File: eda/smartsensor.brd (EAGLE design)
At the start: 33 x 27.9 mm, 46 parts, among them U1 ISL83491SOIC, U2 ATTINY1634, U3 3.3V

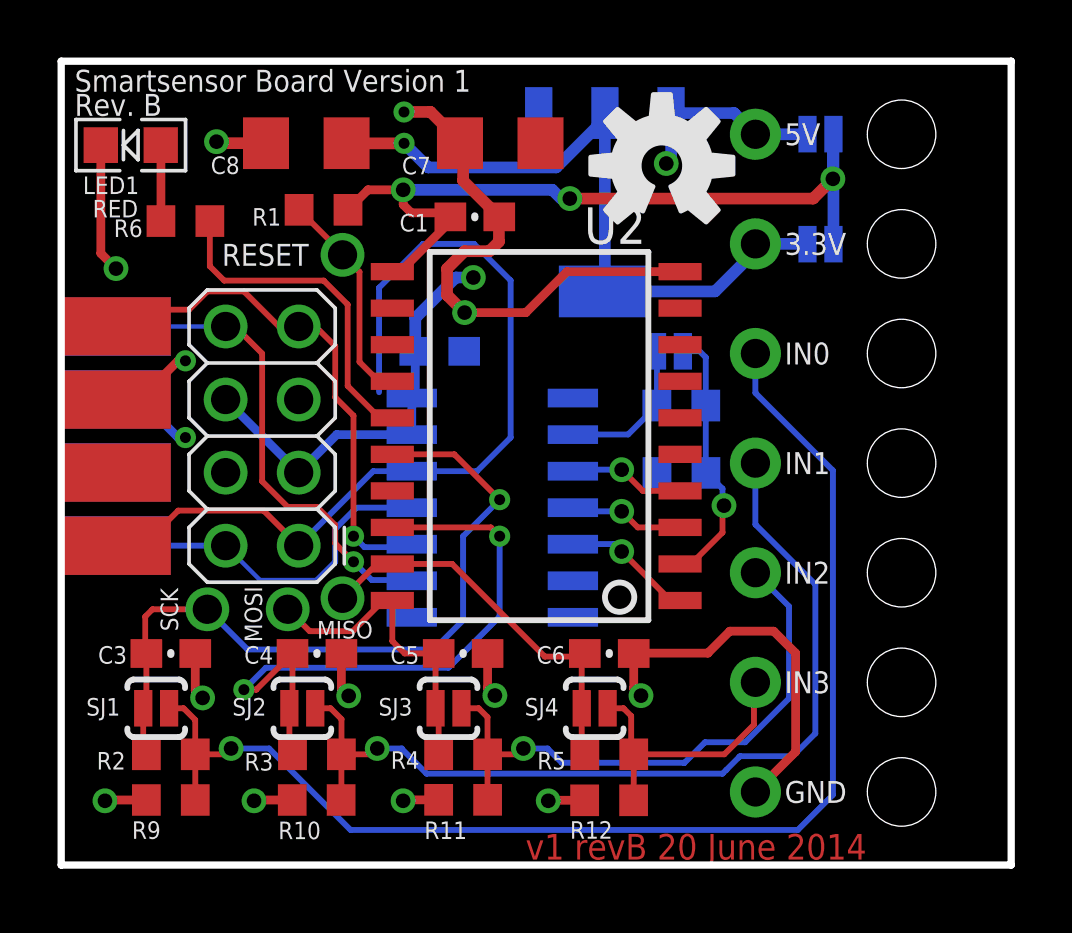
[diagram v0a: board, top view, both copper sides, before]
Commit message: Replaced 2x4 connectors with 2x5's.
On smartsensor, smartsensorPowered, smartsensor_powered_jig, and team_flag.
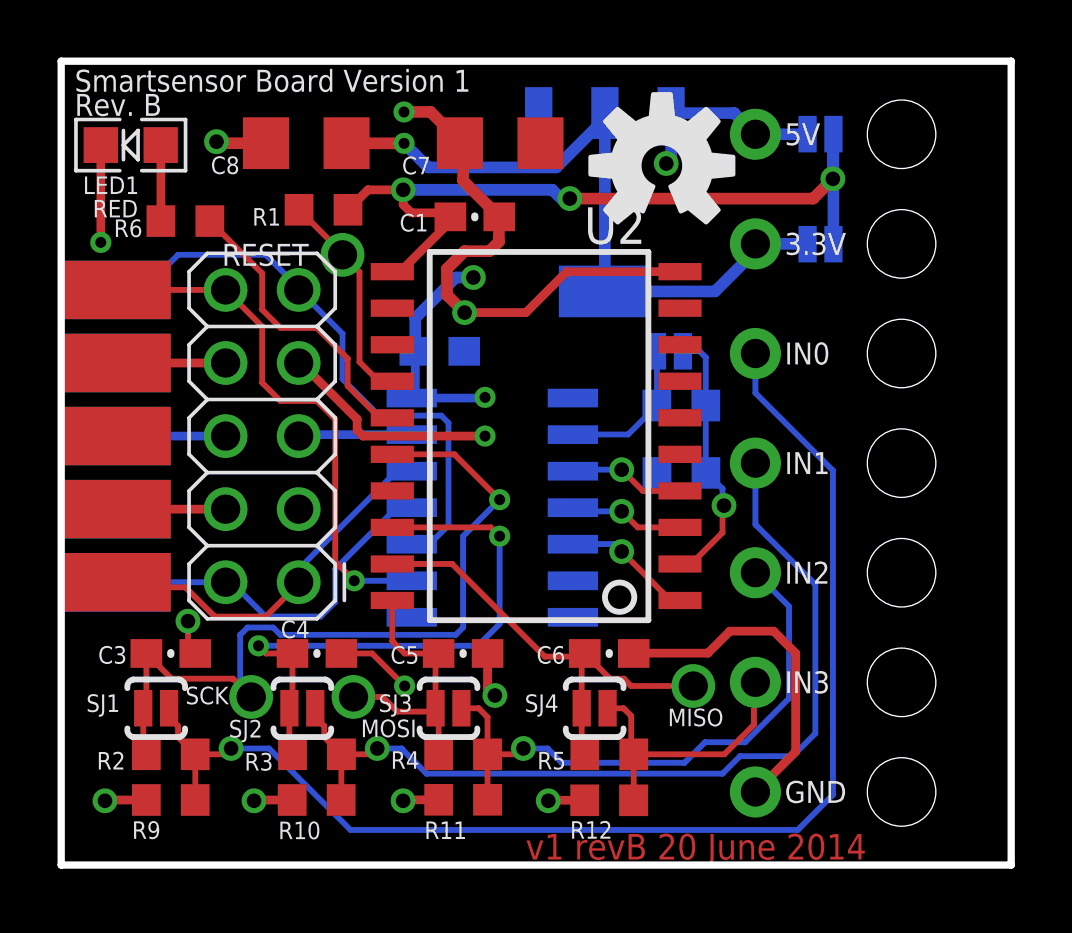
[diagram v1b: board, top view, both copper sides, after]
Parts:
- U$7: value SENSOR_CONPTH -> SENSOR_CON_5PINPTH; device pie:2X4 -> pie:2X5
- U$8: value SENSOR_CONSMD-EDGE -> SENSOR_CON_5PINSMD-EDGE; device pie:2X4-EDGE -> pie:2X5-EDGE
- moved MISO 12.6 mm to (22.0, 6.22)
- moved MOSI 3.81 mm to (10.2, 5.84)
- moved SCK 3.41 mm to (6.60, 5.84)
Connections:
- net 5V: now also U$7.5, U$8.5; no longer U$7.3, U$8.3
- net B_N: now also U$7.9, U$8.9; no longer U$7.7, U$8.7
- net B_P: now also U$7.10, U$8.10; no longer U$7.8, U$8.8
- net GND: now also U$7.3, U$7.7, U$7.8, U$8.3, U$8.7, U$8.8; no longer U$7.5, U$8.5
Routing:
- net A_P: track 31.1 -> 13.2 mm
- net GND: track 52.2 -> 64.0 mm, vias 13 -> 12
- net IO3: track 14.1 -> 16.8 mm
- net B_N: track 18.0 -> 20.6 mm, vias 1 -> 0
- net 5V: track 24.9 -> 22.7 mm
- net IO0: track 26.1 -> 28.2 mm
- net IO1: track 22.4 -> 20.5 mm
- net B_P: track 16.9 -> 18.5 mm
- net IO2: track 11.5 -> 10.2 mm
- net LED: track 11.8 -> 10.5 mm
- net A_N: track 12.5 -> 13.0 mm
